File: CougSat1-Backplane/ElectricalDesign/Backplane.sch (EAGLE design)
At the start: 17 parts, among them J1 CougSat Socket, J10 CougSat Socket, J2 CougSat Socket, J3 CougSat Socket, J4 CougSat Socket, J5 Separation Switch, J6 Separation Switch, J7 CougSat Socket, J8 CougSat Socket, J9 CougSat Socket

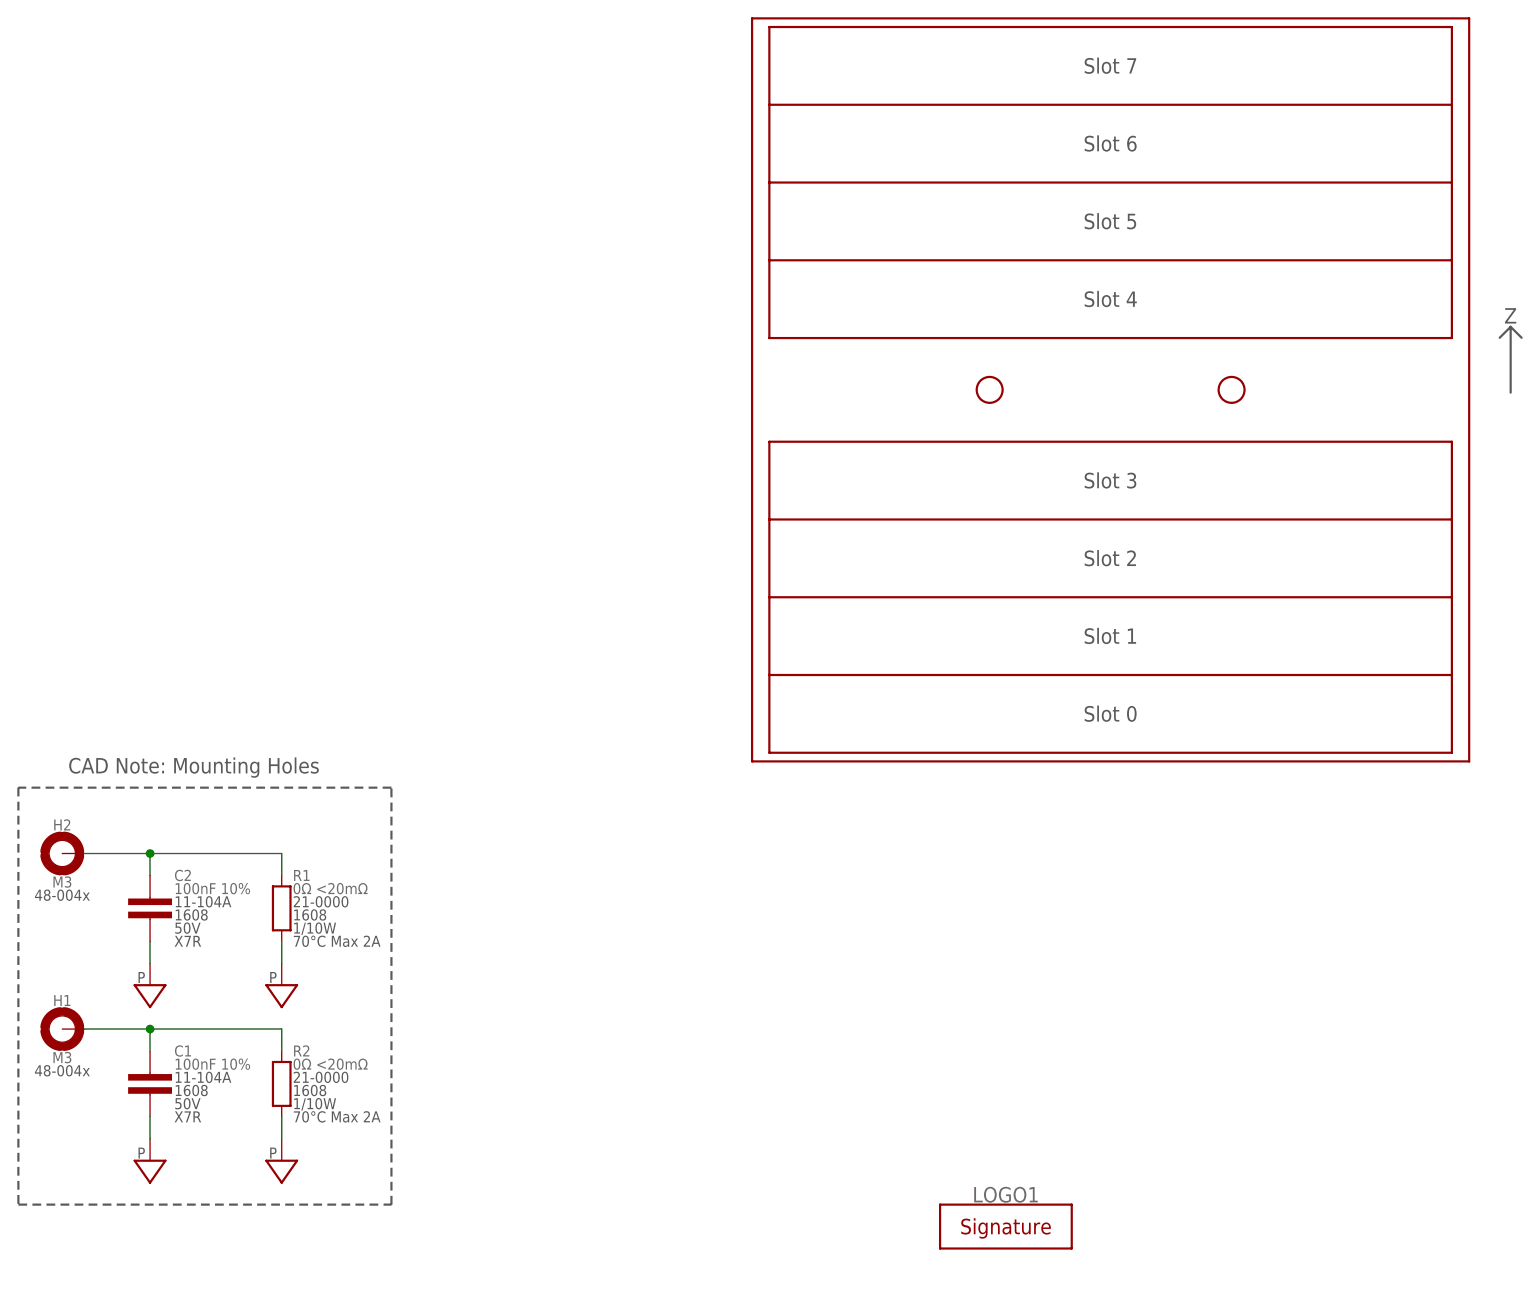
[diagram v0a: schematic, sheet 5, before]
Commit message: Added balancing and silkscreen decals
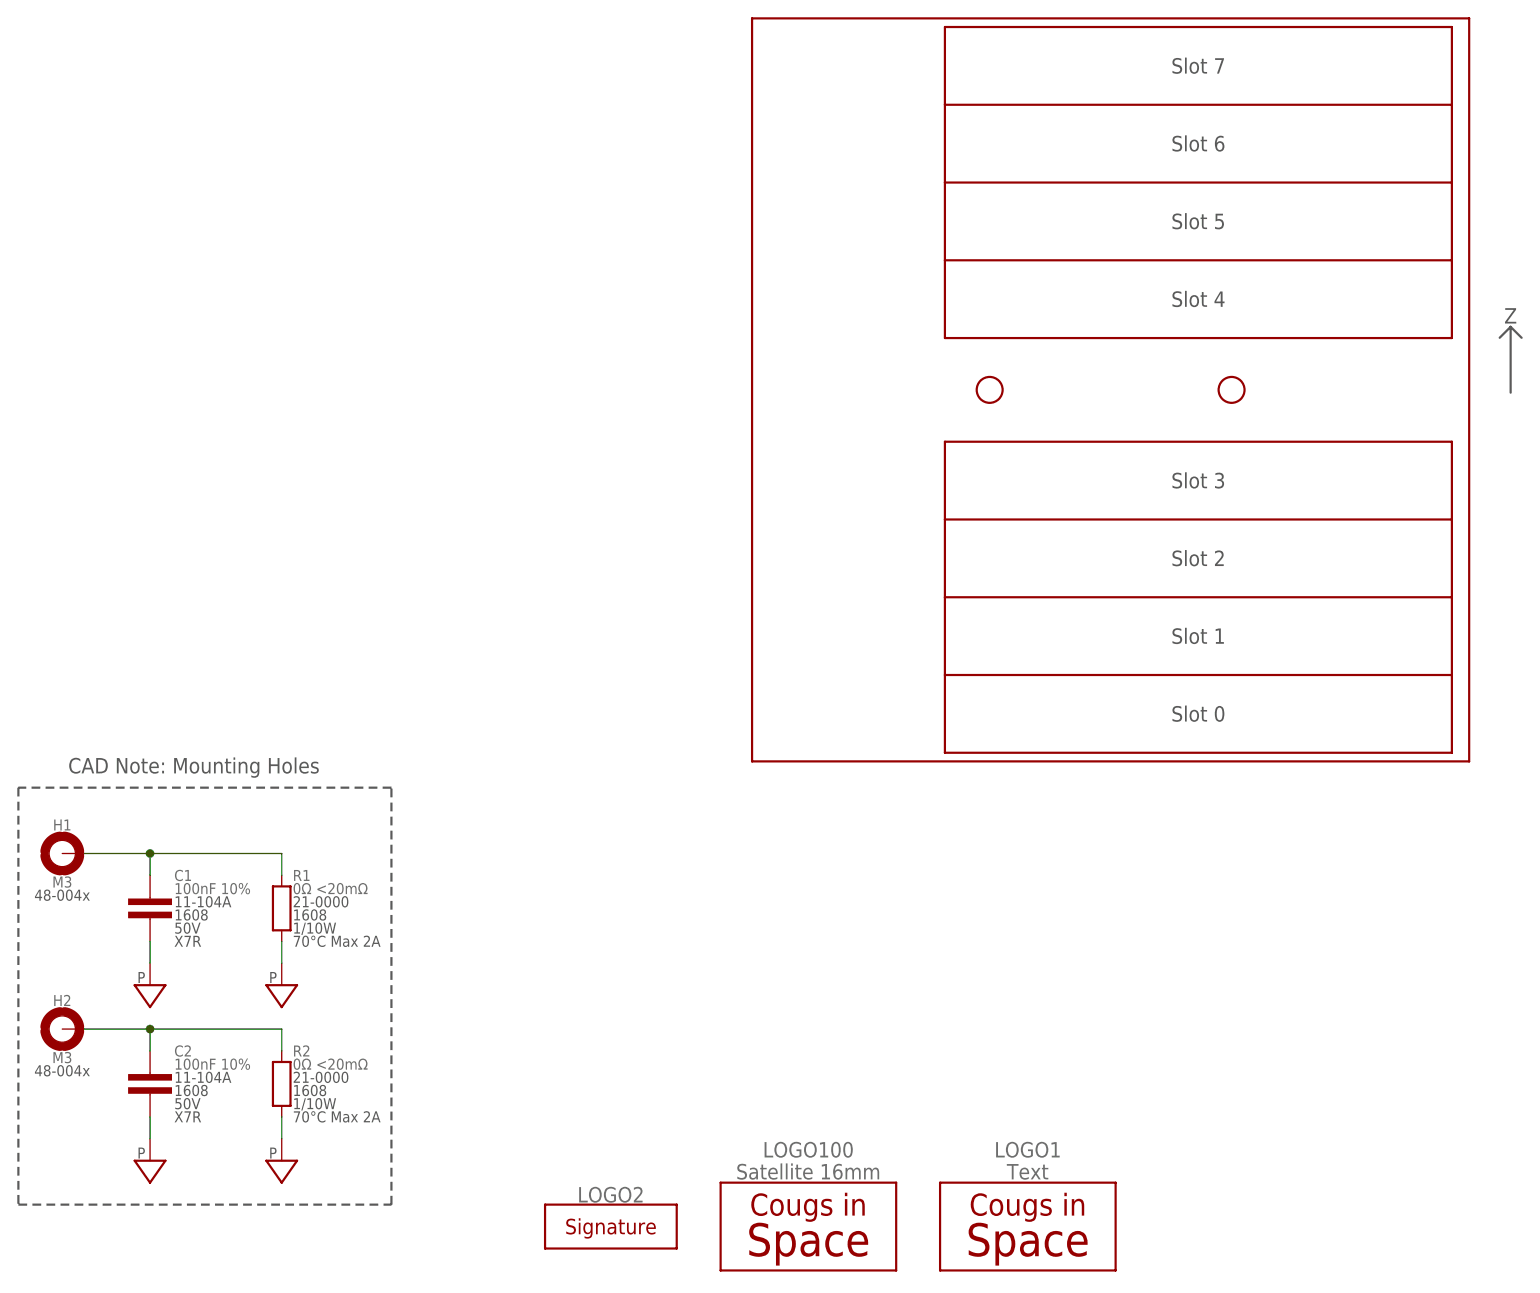
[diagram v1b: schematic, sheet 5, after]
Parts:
- added LOGO100: Satellite 16mm, CougsInSpace-Aesthetics:CIS-LOGO-SATELLITE-16MM
- added LOGO2: SIGNATUREHENDRIK, CougsInSpace-Aesthetics:SIGNATUREHENDRIK
- LOGO1: value SIGNATUREHENDRIK -> Text; device CougsInSpace-Aesthetics:SIGNATUREHENDRIK -> CougsInSpace-Aesthetics:CIS-LOGO-TEXT
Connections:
- net CHASSIS1: now also C1.1, H1.MOUNT; no longer C2.1, H2.MOUNT
- net CHASSIS2: now also C2.1, H2.MOUNT; no longer C1.1, H1.MOUNT
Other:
- moved on the sheet: C1, C2, H1, H2

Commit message: Fixed dimension errors, updated signature
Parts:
- added LOGO3: Satellite 16mm, CougsInSpace-Aesthetics:CIS-LOGO-SATELLITE-16MM
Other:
- moved on the sheet: LOGO2
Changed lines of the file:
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@@
 <attribute name="PART_NUMBER" value="68-0005"/>
 <attribute name="PROJECT" value="CougSat-1: Backplane"/>
-<attribute name="REV" value="3.0.1"/>
+<attribute name="REV" value="3.0.2"/>
 </attributes>
 <variantdefs>
@@
 <part name="LOGO1" library="CougsInSpace-Aesthetics" deviceset="CIS-LOGO" device="-TEXT" value="Text"/>
 <part name="LOGO100" library="CougsInSpace-Aesthetics" deviceset="CIS-LOGO" device="-SATELLITE-16MM" value="Satellite 16mm"/>
+<part name="LOGO3" library="CougsInSpace-Aesthetics" deviceset="CIS-LOGO" device="-SATELLITE-16MM" value="Satellite 16mm"/>
 </parts>
 <sheets>
@@
 <attribute name="SKU" x="36.83" y="27.432" size="1.27" layer="97" align="center-left"/>
 </instance>
-<instance part="LOGO2" gate="G$1" x="73.66" y="10.16" smashed="yes">
-<attribute name="NAME" x="73.66" y="12.954" size="1.778" layer="95" align="bottom-center"/>
+<instance part="LOGO2" gate="G$1" x="121.92" y="27.94" smashed="yes">
+<attribute name="NAME" x="121.92" y="30.734" size="1.778" layer="95" align="bottom-center"/>
 </instance>
 <instance part="LOGO1" gate="G$1" x="121.92" y="10.16" smashed="yes">
@@
 <attribute name="VALUE" x="96.52" y="16.51" size="1.778" layer="96" align="center"/>
 </instance>
+<instance part="LOGO3" gate="G$1" x="96.52" y="27.94" smashed="yes">
+<attribute name="NAME" x="96.52" y="36.83" size="1.778" layer="95" align="center"/>
+<attribute name="VALUE" x="96.52" y="34.29" size="1.778" layer="96" align="center"/>
+</instance>
 </instances>
